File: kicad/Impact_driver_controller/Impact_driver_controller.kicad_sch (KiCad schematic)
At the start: 29 parts, among them Q1 IRFP4468PbF, Q2 IRFP4468PbF, SW1 Reset, U1 Pico, U2 IR2104, U3 LM78M05, U4 LM78M12

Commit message: add current probe
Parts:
- added C10: 1nF, Capacitor_SMD:C_1206_3216Metric_Pad1.33x1.80mm_HandSolder, symbol Device:C
- added C11: 3.3 nF, Capacitor_SMD:C_1206_3216Metric_Pad1.33x1.80mm_HandSolder, symbol Device:C
- added R5, R7: 10k, Resistor_SMD:R_1206_3216Metric_Pad1.30x1.75mm_HandSolder, symbol Device:R
- added R6: 20k, Resistor_SMD:R_1206_3216Metric_Pad1.30x1.75mm_HandSolder, symbol Device:R
- added U5: ACS712xLCTR-30A, Package_SO:SOIC-8_3.9x4.9mm_P1.27mm, symbol Sensor_Current:ACS712xLCTR-30A
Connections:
- net +5V: now also U5.8 (VCC)
- net AGND: now also C10.2, C11.2, R6.2, U5.5 (GND)
- net MOTOR+: now also U5.3 (IP-), U5.4 (IP-); no longer C5.2, Q1.3 (S), Q2.2 (D), U2.6 (VS)
- new net: C10.1, U5.6 (FILTER)
- new net: R5.1, U5.7 (VIOUT)
- new net C_PROBE: C5.2, Q1.3 (S), Q2.2 (D), U2.6 (VS), U5.1 (IP+), U5.2 (IP+)
- new net I_MOTOR: R5.2, R6.1, R7.2
- new net I_MOTOR_F: C11.1, R7.1
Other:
- note added: "Current probe"
- moved on the sheet: F1

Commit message: Add I/O
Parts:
- added Brd1: SSD1306, SSD1306_impact:128x64OLED, symbol SSD1306-128x64_OLED_impact:SSD1306
- added C12: 100uF, Capacitor_SMD:CP_Elec_8x10, symbol Device:C_Polarized
- added C13: 1 uF, Capacitor_SMD:C_1206_3216Metric_Pad1.33x1.80mm_HandSolder, symbol Device:C
- added MOTOR1: Screw_Terminal_01x04, symbol Connector:Screw_Terminal_01x04
- added R10, R8, R9: 10k, Resistor_SMD:R_1206_3216Metric_Pad1.30x1.75mm_HandSolder, symbol Device:R
- added RV_SPEED1: Screw_Terminal_01x03, TerminalBlock_MetzConnect:TerminalBlock_MetzConnect_Type101_RT01603HBWC_1x03_P5.08mm_Horizontal, symbol Connector:Screw_Terminal_01x03
- added RV_SPEED2: RV_OFFBOARD_10k, symbol Device:R_Potentiometer
- added SW_MODE1: SW_OFFBOARD, symbol Switch:SW_DPST_x2
- added SW_MODE2: Screw_Terminal_01x02, TerminalBlock_MetzConnect:TerminalBlock_MetzConnect_Type101_RT01602HBWC_1x02_P5.08mm_Horizontal, symbol Connector:Screw_Terminal_01x02
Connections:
- net +3.3V: now also Brd1.2 (VCC), R10.1, R9.1, RV_SPEED1.1 (Pin_1), RV_SPEED2.1
- net +Vlogic: now also C12.1
- net AGND: now also C13.2, RV_SPEED1.3 (Pin_3), RV_SPEED2.3
- net ENABLE: now also U1.21 (GPIO16)
- net GND: now also Brd1.1 (GND), C12.2, MOTOR1.3 (Pin_3), MOTOR1.4 (Pin_4), SW_MODE1.2 (B), SW_MODE2.1 (Pin_1)
- net I_MOTOR_F: now also U1.32 (GPIO27_ADC1)
- net MOTOR+: now also MOTOR1.1 (Pin_1), MOTOR1.2 (Pin_2)
- net PWM: now also U1.22 (GPIO17)
- net SW_MODE: now reaches U1.12 (GPIO9)
- net SW_MODE: now also SW_MODE1.1 (A), SW_MODE2.2 (Pin_2)
- net RV_SPEED_F: now reaches U1.34 (GPIO28_ADC2)
- net RV_SPEED_F: now also C13.1, R8.1
- net SDA: now reaches U1.6 (GPIO4)
- net SDA: now also Brd1.4 (SDA), R9.2
- net SCL: now reaches U1.7 (GPIO5)
- net SCL: now also Brd1.3 (SCL), R10.2
- new net RV_SPEED: R8.2, RV_SPEED1.2 (Pin_2), RV_SPEED2.2
- no-connect marks 3 -> 30
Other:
- note added: "Filters"
- note added: "I/O"
- moved on the sheet: C1, C10, C11, C2, C3, C4, C5, C6, C7, C8, C9, D1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

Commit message: Add MCU module
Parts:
- removed C12: 100uF, Capacitor_SMD:CP_Elec_8x10, symbol Device:C_Polarized
- removed C6, C8: 0.33 uF, Capacitor_SMD:C_1206_3216Metric_Pad1.33x1.80mm_HandSolder, symbol Device:C
- removed C7, C9: 0.1 uF, Capacitor_SMD:C_1206_3216Metric_Pad1.33x1.80mm_HandSolder, symbol Device:C
- removed D3: SS34A, Diode_SMD:D_SMB-SMC_Universal_Handsoldering, symbol Device:D_Schottky
- removed D4: LED, Diode_SMD:D_1206_3216Metric_Pad1.42x1.75mm_HandSolder, symbol Device:LED
- removed F1: 30-40 A, Fuse:Fuse_Blade_ATO_directSolder, symbol Device:Fuse
- removed F2: 1A, Fuse:Fuse_Blade_ATO_directSolder, symbol Device:Fuse
- removed R4: 1k, Resistor_SMD:R_1206_3216Metric_Pad1.30x1.75mm_HandSolder, symbol Device:R
- removed SW_PWR2: SW_OFFBOARD, symbol Switch:SW_DPST_x2
- removed U3: LM78M05, Package_TO_SOT_SMD:TO-252-2, symbol Regulator_Linear:LM78M05_TO252
- removed U4: LM78M12, Package_TO_SOT_SMD:TO-252-2, symbol Regulator_Linear:LM7812_TO220
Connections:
- net Power supply/+V: now reaches IN_POWER1.1 (Pin_1), IN_POWER1.2 (Pin_2)
- net Power supply/+V: no longer SW_PWR1.2 (Pin_2)
- net Power supply/PWR_BTNB: now reaches SW_PWR1.1 (Pin_1)
- new net Power supply/PWR_BTNA: SW_PWR1.2 (Pin_2)
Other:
- added sheet Power supply (power_supply.kicad_sch)
- note removed: "Power"

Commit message: Main board schematic
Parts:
- removed Brd1: SSD1306, SSD1306_impact:128x64OLED, symbol SSD1306-128x64_OLED_impact:SSD1306
- removed C1: 100 nF - 250 V, symbol Device:C
- removed C10: 1nF, Capacitor_SMD:C_1206_3216Metric_Pad1.33x1.80mm_HandSolder, symbol Device:C
- removed C11: 3.3 nF, Capacitor_SMD:C_1206_3216Metric_Pad1.33x1.80mm_HandSolder, symbol Device:C
- removed C13: 1 uF, Capacitor_SMD:C_1206_3216Metric_Pad1.33x1.80mm_HandSolder, symbol Device:C
- removed C2: 220uF - 100 V, symbol Device:C_Polarized
- removed C3: 100 nF, symbol Device:C
- removed C4, C5: 10uF, symbol Device:C_Polarized
- removed D1: D_Schottky, Diode_SMD:D_SOD-123, symbol Device:D_Schottky
- removed D2: D, symbol Device:D
- removed MOTOR1: Screw_Terminal_01x04, symbol Connector:Screw_Terminal_01x04
- removed Q1, Q2: IRFP4468PbF, Package_TO_SOT_THT:TO-247-3_Vertical, symbol Transistor_FET:IRFP4468PbF
- removed R1, R2: 10R, symbol Device:R
- removed R10, R5, R7, R8, R9: 10k, Resistor_SMD:R_1206_3216Metric_Pad1.30x1.75mm_HandSolder, symbol Device:R
- removed R3: 10k, symbol Device:R
- removed R6: 20k, Resistor_SMD:R_1206_3216Metric_Pad1.30x1.75mm_HandSolder, symbol Device:R
- removed RV_SPEED1: Screw_Terminal_01x03, TerminalBlock_MetzConnect:TerminalBlock_MetzConnect_Type101_RT01603HBWC_1x03_P5.08mm_Horizontal, symbol Connector:Screw_Terminal_01x03
- removed RV_SPEED2: RV_OFFBOARD_10k, symbol Device:R_Potentiometer
- removed SW1: Reset, symbol Switch:SW_Push
- removed SW_MODE1: SW_OFFBOARD, symbol Switch:SW_DPST_x2
- removed SW_MODE2: Screw_Terminal_01x02, TerminalBlock_MetzConnect:TerminalBlock_MetzConnect_Type101_RT01602HBWC_1x02_P5.08mm_Horizontal, symbol Connector:Screw_Terminal_01x02
- removed U1: Pico, MCU_RaspberryPi_and_Boards_impact:RPi_Pico_SMD_TH, symbol MCU_RaspberryPi_and_Boards_impact:Pico
- removed U2: IR2104, Package_SO:SOIC-8_3.9x4.9mm_P1.27mm, symbol Driver_FET:IR2104
- removed U5: ACS712xLCTR-30A, Package_SO:SOIC-8_3.9x4.9mm_P1.27mm, symbol Sensor_Current:ACS712xLCTR-30A
- added U10: Control_panel_module, modules:control_panel_module, symbol control_panel_module:control_panel_module
- added U6: MCU_module, MCU_module:MCU_module, symbol MCU_module:MCU_module
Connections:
- net +3.3V: now also U10.7 (+3.3V), U6.36 (3V3)
- net +5V: now also U6.39 (+5V)
- net +VDD: now also U10.1 (Vin)
- net AGND: now also U10.10 (AGND), U6.33 (AGND)
- net GND: now also U10.2 (GND), U6.18 (GND)
- net SCL: now also U10.9 (SCL), U6.7 (GPIO5)
- net SDA: now also U10.8 (SDA), U6.6 (GPIO4)
- net Power supply/+V renamed Power supply/+V_IN
- new net: U10.11 (RV_SPEED), U6.32 (F1)
- new net: U10.3 (SW_MODE), U6.24 (GPIO18)
- new net: U10.4 (LED_ERR), U6.21 (GPIO16)
- new net: U10.5 (LED_STATUS), U6.22 (GPIO17)
- new net Current probe/I_MEAS: U6.34 (F2)
- new net Drivers/EN: U6.10 (GPIO7)
- new net Drivers/FAULT_1: U6.14 (GPIO10)
- new net Drivers/FAULT_2: U6.15 (GPIO11)
- new net Drivers/FAULT_3: U6.16 (GPIO12)
- new net Drivers/FAULT_4: U6.17 (GPIO13)
- new net Drivers/FAULT_5: U6.19 (GPIO14)
- new net Drivers/FAULT_6: U6.20 (GPIO15)
- new net Drivers/PH: U6.11 (GPIO8)
- new net Drivers/SLEEP: U6.12 (GPIO9)
- no-connect marks 30 -> 18
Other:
- added sheet Current probe (current_probe.kicad_sch)
- added sheet Drivers (Drivers.kicad_sch)
- sheet Power supply ports: added +VDD_OUT, +V_IN; removed +V
- note removed: "Current probe"
- note removed: "Filters"
- note removed: "Half bridge"
- note removed: "I/O"
- note removed: "Microcontroller"
- moved on the sheet: IN_POWER1, SW_PWR1

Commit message: main board silkscreen
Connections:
- no-connect marks 18 -> 19
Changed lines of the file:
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@@
+	)
+	(no_connect
+		(at 181.61 26.67)
 	)
 	(no_connect

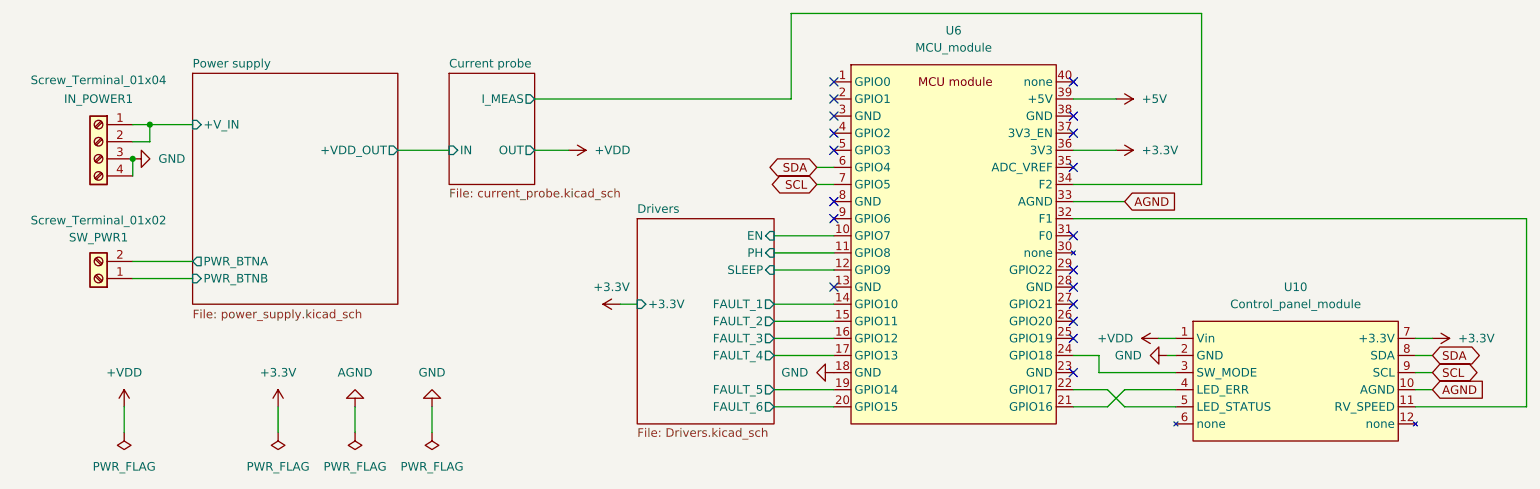
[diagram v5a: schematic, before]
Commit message: Connector for bigger current, control module 2
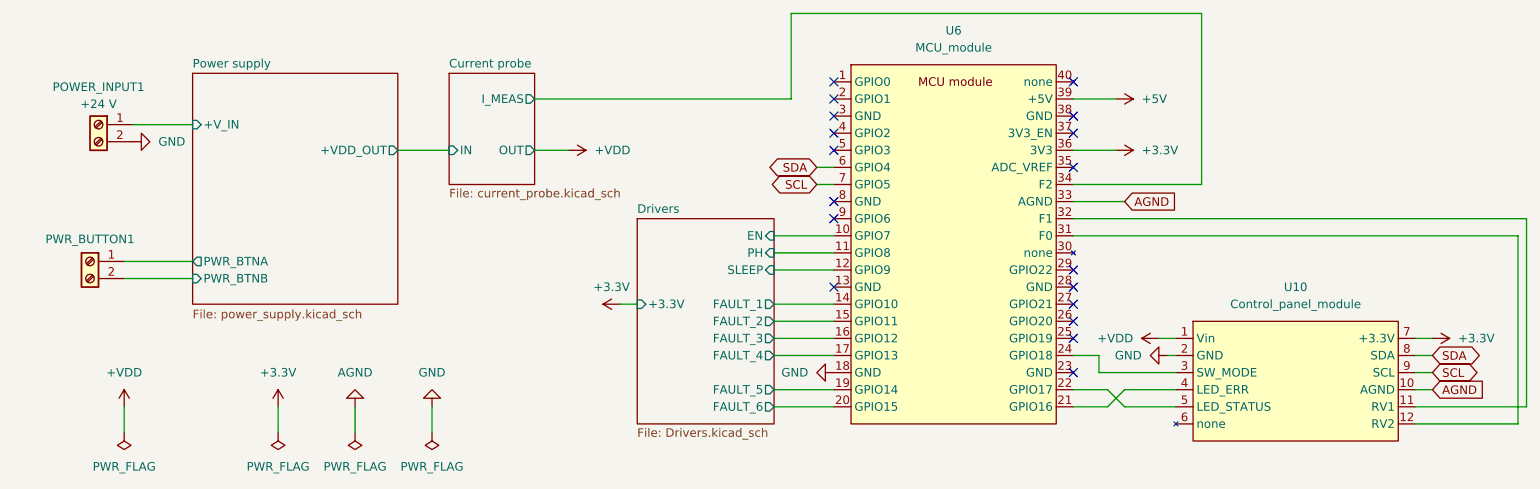
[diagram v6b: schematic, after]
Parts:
- removed IN_POWER1: Screw_Terminal_01x04, TerminalBlock_MetzConnect:TerminalBlock_MetzConnect_Type101_RT01604HBWC_1x04_P5.08mm_Horizontal, symbol Connector:Screw_Terminal_01x04
- removed SW_PWR1: Screw_Terminal_01x02, TerminalBlock_MetzConnect:TerminalBlock_MetzConnect_Type101_RT01602HBWC_1x02_P5.08mm_Horizontal, symbol Connector:Screw_Terminal_01x02
- added POWER_INPUT1: +24 V, T-DEAN_impact:DEANS, symbol Connector:Screw_Terminal_01x02
- added PWR_BUTTON1: ~, T-DEAN_impact:DEANS, symbol Connector:Screw_Terminal_01x02
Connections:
- net GND: now also POWER_INPUT1.2 (Pin_2)
- net Power supply/+V_IN: now also POWER_INPUT1.1 (Pin_1)
- net Power supply/PWR_BTNA: now also PWR_BUTTON1.1 (Pin_1)
- net Power supply/PWR_BTNB: now also PWR_BUTTON1.2 (Pin_2)
- net at U10.12 (RV2): now also U6.31 (F0)
- no-connect marks 19 -> 18

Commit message: Add part numbers
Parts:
- J1: renamed from POWER_INPUT1; value +24 V -> 1x2 TDEAN
- J2: renamed from PWR_BUTTON1; value ~ -> 1x2 TDEAN
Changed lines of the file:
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@@
 		(on_board yes)
 		(dnp no)
-		(property "Reference" "PWR_BUTTON1"
+		(property "Reference" "J2"
 			(at 35.56 50.038 0)
 			(effects
@@
 			)
 		)
-		(property "Value" "~"
+		(property "Value" "1x2 TDEAN"
 			(at 35.56 61.976 0)
 			(effects
@@
 			)
 		)
-		(property "Description" "Generic screw terminal, single row, 01x02, script generated (kicad-library-utils/schlib/autogen/connector/)"
+		(property "Description" "CUSTOM"
 			(at 35.56 53.34 0)
 			(effects
@@
 			(project "Impact_driver_controller"
 				(path "/306f6389-4643-4955-9a33-8107bbcd4995"
-					(reference "PWR_BUTTON1")
+					(reference "J2")
 					(unit 1)
 				)
@@
 		(on_board yes)
 		(dnp no)
-		(property "Reference" "POWER_INPUT1"
+		(property "Reference" "J1"
 			(at 36.83 27.432 0)
 			(effects
@@
 			)
 		)
-		(property "Value" "+24 V"
+		(property "Value" "1x2 TDEAN"
 			(at 36.83 29.972 0)
 			(effects
@@
 			)
 		)
-		(property "Description" "Generic screw terminal, single row, 01x02, script generated (kicad-library-utils/schlib/autogen/connector/)"
+		(property "Description" "CUSTOM"
 			(at 36.83 33.02 0)
 			(effects
@@
 			(project "Impact_driver_controller"
 				(path "/306f6389-4643-4955-9a33-8107bbcd4995"
-					(reference "POWER_INPUT1")
+					(reference "J1")
 					(unit 1)
 				)
